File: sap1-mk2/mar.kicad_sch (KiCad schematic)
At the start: 0 parts

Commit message: added A Register, B Register, Instruction Register, and Memory Address Register
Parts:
- added C21, C22: 0.1μF, symbol Device:C_Small
- added D26, D27, D28, D29: YELLOW, symbol Device:LED
- added D30: RED, symbol Device:LED
- added D31: GREEN, symbol Device:LED
- added R32, R33, R34, R35: 220, symbol Device:R
- added R36, R37: 1K, symbol Device:R
- added SW3: SW_DIP_x04, symbol Switch:SW_DIP_x04
- added SW4: SW_SPDT, symbol Switch:SW_SPDT
- added U16: 74LS173, symbol 74xx:74LS173
- added U17: 74LS157, symbol 74xx:74LS157
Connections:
- new net: D28.1 (K), R34.1
- new net: D30.2 (A), R36.1
- new net: D31.1 (K), SW4.3 (C)
- new net: D31.2 (A), R37.1
- new net: U16.5 (Q2), U17.10 (I1c)
- new net: SW3.2, U17.11 (I0c)
- new net: U16.6 (Q3), U17.13 (I1d)
- new net: SW3.1, U17.14 (I0d)
- new net: SW3.5, U17.2 (I0a)
- new net: U16.3 (Q0), U17.3 (I1a)
- new net: SW3.6, U17.5 (I0b)
- new net: U16.4 (Q1), U17.6 (I1b)
- new net: D26.1 (K), R32.1
- new net: D29.1 (K), R35.1
- new net: D27.1 (K), R33.1
- new net +5V: C21.2, C22.1, R36.2, R37.2, U16.16 (VCC), U17.16 (VCC)
- new net A0: D29.2 (A), U17.12 (Zd)
- new net A1: D28.2 (A), U17.9 (Zc)
- new net A2: D27.2 (A), U17.7 (Zb)
- new net A3: D26.2 (A), U17.4 (Za)
- new net BUS_0: U16.11 (D3)
- new net BUS_1: U16.12 (D2)
- new net BUS_2: U16.13 (D1)
- new net BUS_3: U16.14 (D0)
- new net CLK: U16.7 (Cp)
- new net CLR: U16.15 (Mr)
- new net GND: C21.1, C22.2, R32.2, R33.2, R34.2, R35.2, SW3.3, SW3.4, SW3.7, SW3.8, SW4.2 (B), U16.1 (Oe1), U16.2 (Oe2), U16.8 (GND), U17.15 (E), U17.8 (GND)
- new net PROG: D30.1 (K), SW4.1 (A), U17.1 (S)
- new net ~{MI}: U16.10 (E2), U16.9 (E1)
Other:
- title: (none) -> Memory Address Register

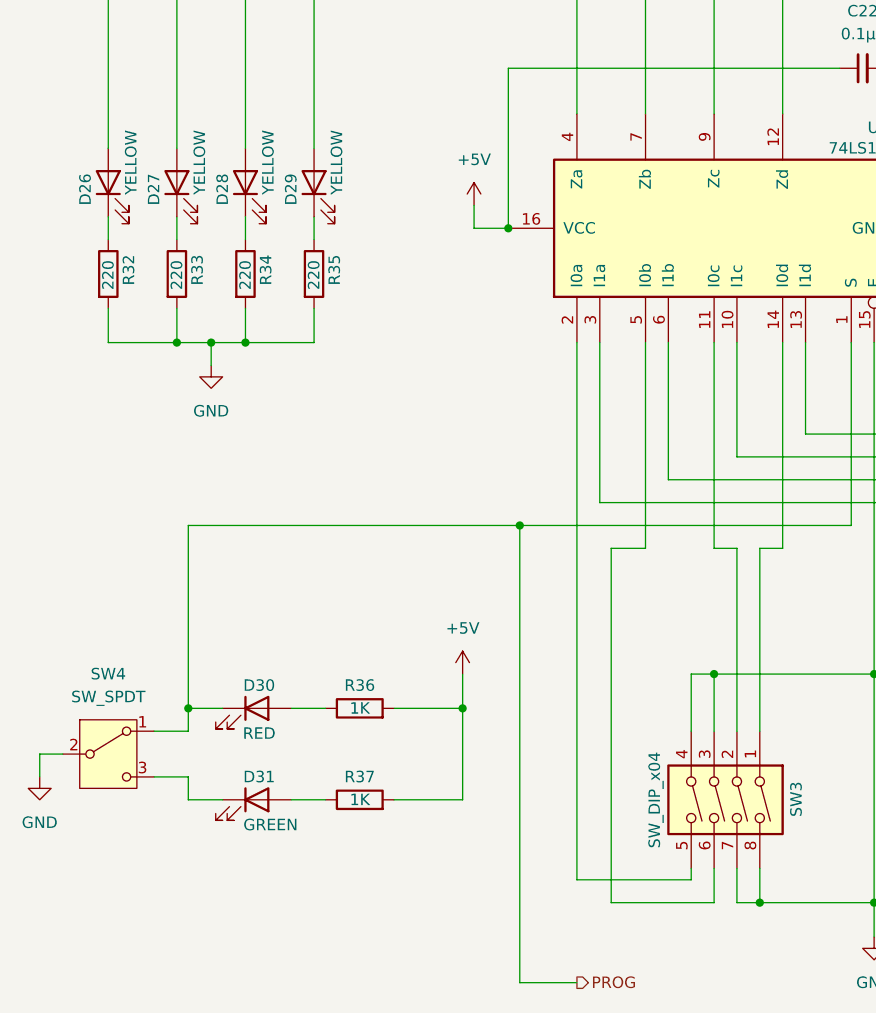
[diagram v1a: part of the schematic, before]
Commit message: added ALU + some minor tweaks
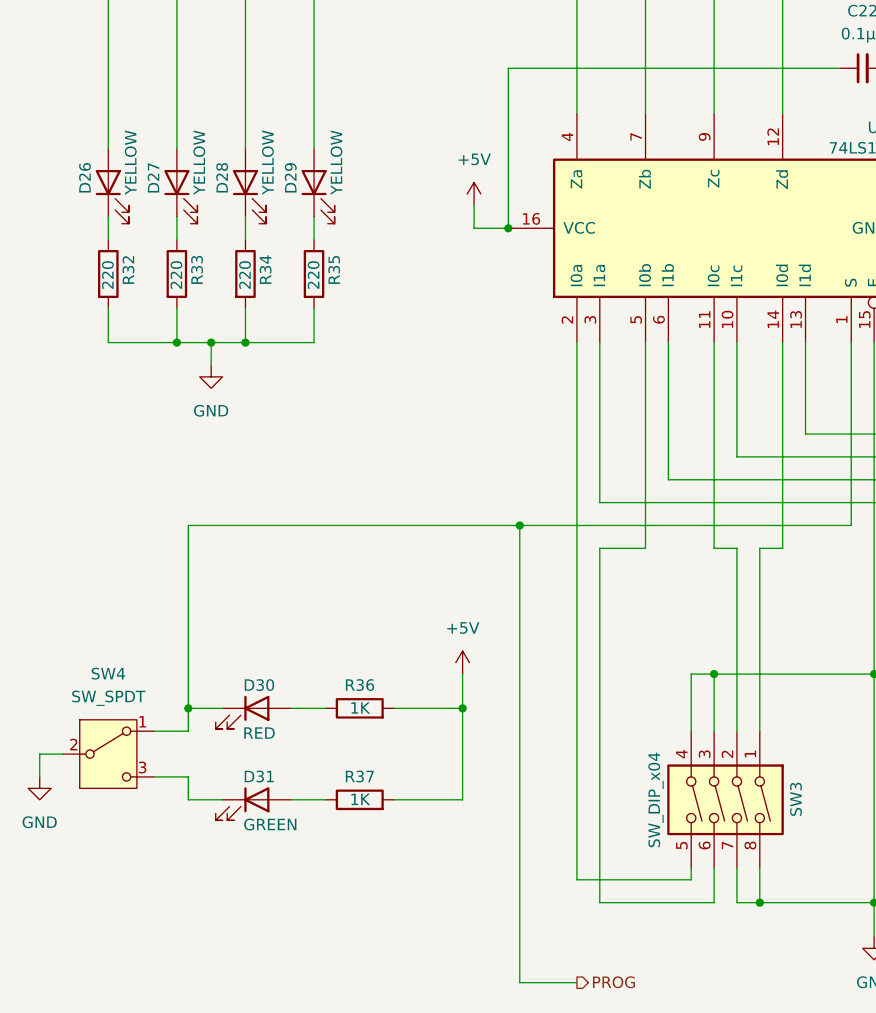
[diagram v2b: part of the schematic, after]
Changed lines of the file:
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@@
 	(wire
 		(pts
-			(xy 120.65 148.59) (xy 132.08 148.59)
-		)
-		(stroke
-			(width 0)
-			(type default)
-		)
-	)
-	(wire
-		(pts
-			(xy 120.65 109.22) (xy 120.65 148.59)
+			(xy 119.38 148.59) (xy 132.08 148.59)
+		)
+		(stroke
+			(width 0)
+			(type default)
+		)
+	)
+	(wire
+		(pts
+			(xy 119.38 109.22) (xy 119.38 148.59)
 		)
 		(stroke
@@
 	(wire
 		(pts
-			(xy 124.46 109.22) (xy 120.65 109.22)
+			(xy 124.46 109.22) (xy 119.38 109.22)
 		)
 		(stroke
@@
 		(dnp no)
 		(property "Reference" "D29"
-			(at 85.09 67.564 0)
+			(at 85.09 66.294 0)
 			(show_name no)
 			(do_not_autoplace no)
@@
 		(dnp no)
 		(property "Reference" "D27"
-			(at 69.85 67.564 0)
+			(at 69.85 66.294 0)
 			(show_name no)
 			(do_not_autoplace no)
@@
 		(dnp no)
 		(property "Reference" "D26"
-			(at 62.23 67.564 0)
+			(at 62.23 66.294 0)
 			(show_name no)
 			(do_not_autoplace no)
@@
 		(dnp no)
 		(property "Reference" "D28"
-			(at 77.47 67.564 0)
-			(show_name no)
-			(do_not_autoplace no)
+			(at 77.47 66.294 0)
+			(show_name no)
+			(do_not_autoplace no)
